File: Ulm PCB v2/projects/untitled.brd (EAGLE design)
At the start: 56.6 x 49.2 mm, 26 parts, among them U1 FT232RLSSOP, U2 MCP73831, U3 SPX3819-3.3, U4 RFM69HCW, X2 USB-SMD-NS

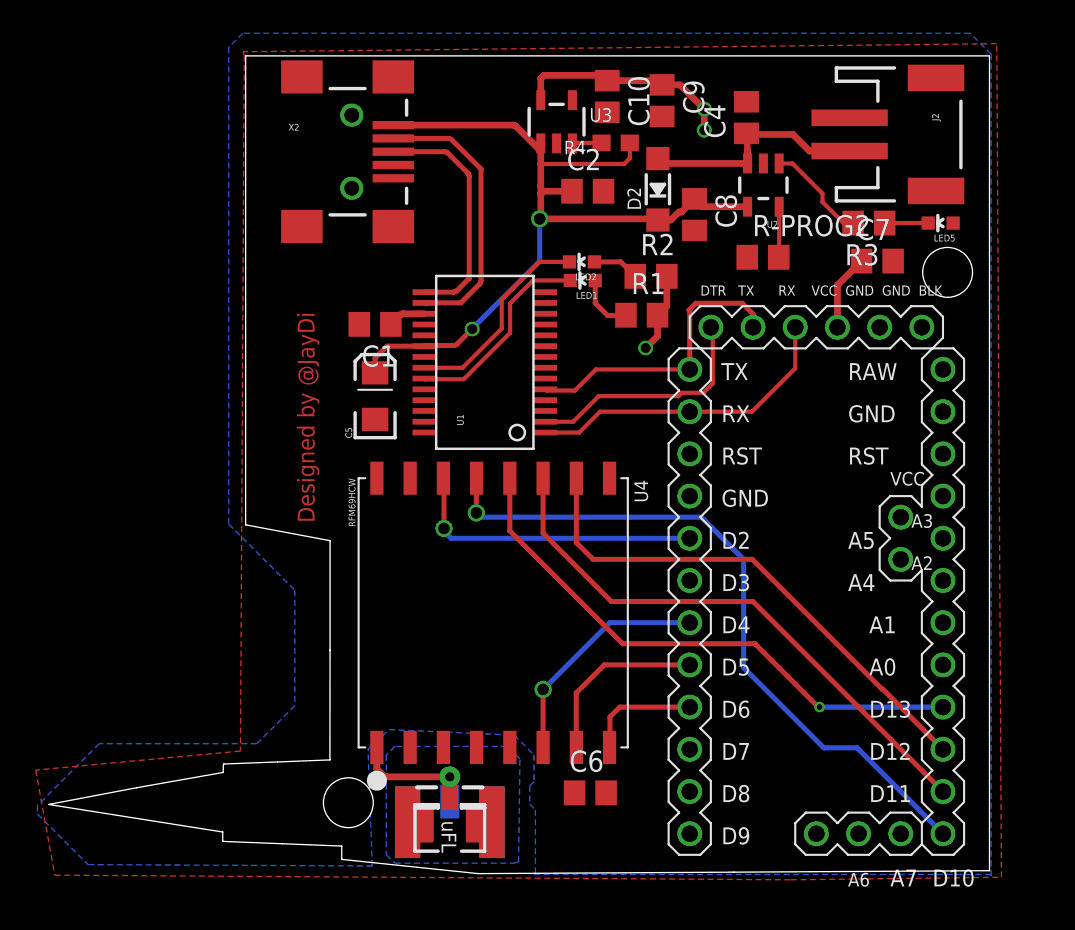
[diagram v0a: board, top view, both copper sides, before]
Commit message: corrected DRC-Errors. ToDo: Right USB Slot, Diode vs. Jumper
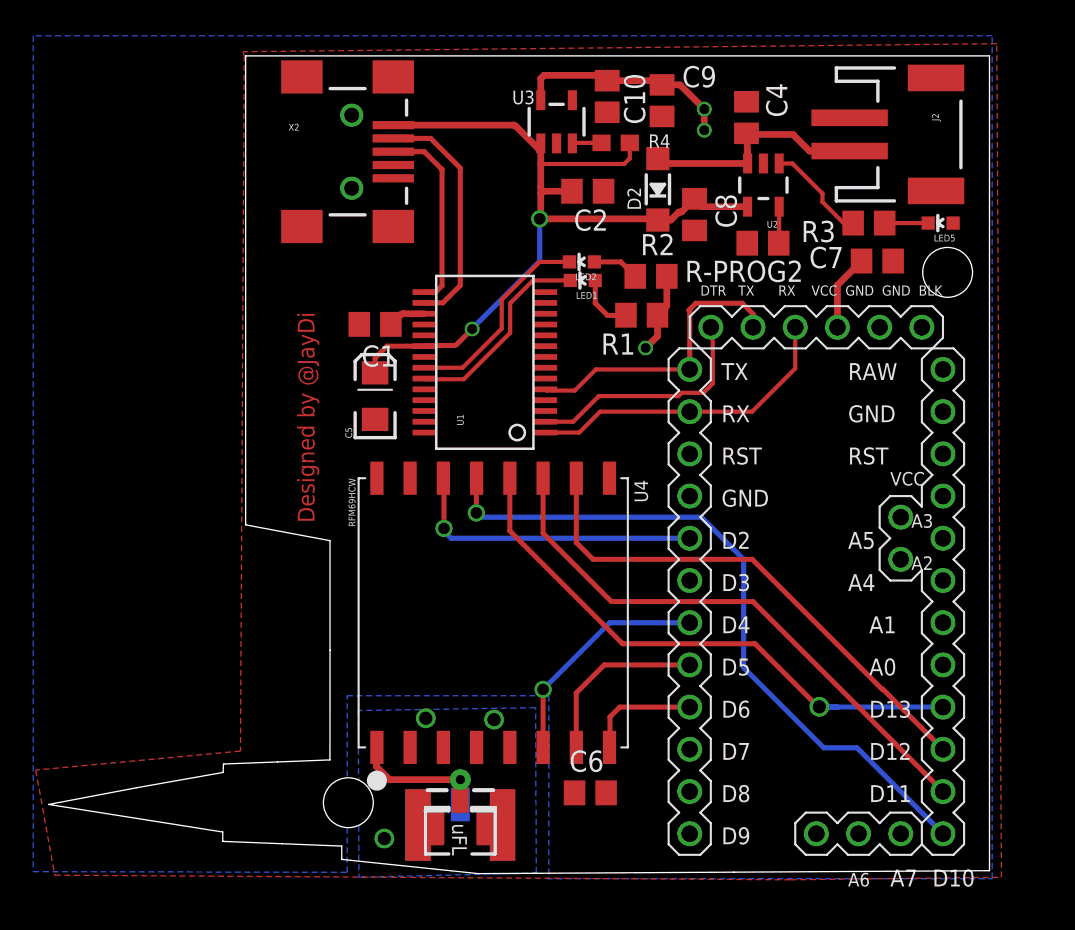
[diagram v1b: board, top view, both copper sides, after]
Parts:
- moved R-PROG2 0.85 mm to (43.9, 39.2)
- moved J$2 0.66 mm to (25.7, 1.81)
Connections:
- removed net N$4: J$2.ANT1, J$2.ANT2, J$2.ANT3
- new net ANT: J$2.ANT1, J$2.ANT2, J$2.ANT3, U4.1P
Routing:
- net ANT: track 0.00 -> 9.27 mm
- net N$4: track 8.95 -> 0.00 mm
- net USB_D+: track 14.4 -> 11.7 mm
- net USB_D-: track 16.8 -> 14.5 mm
- net SCL: track 33.6 -> 34.8 mm
- net LOL: track 3.04 -> 2.20 mm
- net GND: vias 0 -> 3

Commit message: Final Final
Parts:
- added D3: MBR120, microbuilder:SOD-123
- moved C2 4.78 mm to (28.8, 41.1), turned to 270 degrees
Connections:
- removed net 5V: C2.1, C5.A, C8.1, D2.C, R4.1, U1.20, U2.4, U3.1, X2.VBUS
- new net V5: C8.1, D2.C, D3.C, R4.1, U2.4, U3.1
- new net VBUS: C2.1, C5.A, D3.A, U1.20, X2.VBUS
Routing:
- net 5V: track 51.7 -> 0.00 mm, vias 2 -> 0
- net VBUS: track 0.00 -> 27.8 mm, vias 0 -> 2
- net V5: track 0.00 -> 26.5 mm
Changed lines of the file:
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@@
 <elements>
 <element name="C1" library="rcl" library_urn="urn:adsk.eagle:library:334" package="C0805" value="0.1uF" x="20.574" y="34.29" rot="R180"/>
-<element name="C2" library="rcl" library_urn="urn:adsk.eagle:library:334" package="C0805" value="0.1uF" x="33.3733875" y="42.30069375" smashed="yes">
-<attribute name="NAME" x="32.526803125" y="39.9293" size="1.27" layer="25"/>
-<attribute name="VALUE" x="32.1033875" y="39.76069375" size="1.27" layer="27"/>
+<element name="C2" library="rcl" library_urn="urn:adsk.eagle:library:334" package="C0805" value="0.1uF" x="28.75131875" y="41.063496875" smashed="yes" rot="R270">
+<attribute name="NAME" x="26.379925" y="41.91008125" size="1.27" layer="25" rot="R270"/>
+<attribute name="VALUE" x="26.21131875" y="42.333496875" size="1.27" layer="27" rot="R270"/>
 </element>
 <element name="C5" library="SparkFun" package="EIA3216" value="10uF" x="20.574" y="29.972" rot="R90"/>
@@
 <element name="J$2" library="_c2h" package="SMA_UFL_PAD_TINY" value="ANTENNATINY" x="25.704928125" y="1.811834375" rot="R270"/>
 <element name="U4" library="microbuilder" package="RFMHCW_SMT" value="RFM69HCW" x="27.683234375" y="16.9316375" rot="R270"/>
+<element name="D3" library="microbuilder" package="SOD-123" value="MBR120" x="25.997865625" y="47.422815625" rot="R180"/>
 </elements>
 <signals>
@@
 <contactref element="U1" pad="4"/>
 </signal>
-<signal name="5V">
-<contactref element="U1" pad="20"/>
-<contactref element="C5" pad="A"/>
-<contactref element="C2" pad="1"/>
-<contactref element="X2" pad="VBUS"/>
-<contactref element="C8" pad="1"/>
-<contactref element="U3" pad="1"/>
-<contactref element="D2" pad="C"/>
-<contactref element="R4" pad="1"/>
-<contactref element="U2" pad="4"/>
-<wire x1="30.513953125" y1="45.213946875" x2="30.546" y2="45.1819" width="0.4064" layer="1"/>
-<wire x1="30.546" y1="44.716071875" x2="30.546" y2="45.1819" width="0.4064" layer="1"/>
-<wire x1="30.546" y1="44.716071875" x2="30.546" y2="43.942" width="0.4064" layer="1"/>
-<wire x1="30.546" y1="43.942" x2="30.546" y2="42.606" width="0.4064" layer="1"/>
-<wire x1="35.902" y1="45.212" x2="35.902" y2="44.284" width="0.254" layer="1"/>
-<wire x1="35.902" y1="44.284" x2="35.56" y2="43.942" width="0.254" layer="1"/>
-<wire x1="35.56" y1="43.942" x2="30.546" y2="43.942" width="0.254" layer="1"/>
-<wire x1="20.574" y1="31.372" x2="20.657" y2="31.455" width="0.254" layer="1"/>
-<wire x1="30.48" y1="42.54" x2="30.546" y2="42.606" width="0.3048" layer="1"/>
-<via x="30.48" y="40.64" extent="1-16" drill="0.7"/>
-<wire x1="39.798" y1="41.835359375" x2="39.798" y2="41.844" width="0.4064" layer="1"/>
-<wire x1="42.992" y1="41.3719" x2="40.261459375" y2="41.3719" width="0.4064" layer="1"/>
-<wire x1="40.261459375" y1="41.3719" x2="39.798" y2="41.835359375" width="0.4064" layer="1"/>
-<wire x1="38.85861875" y1="41.0512" x2="39.013840625" y2="41.0512" width="0.4064" layer="1"/>
-<wire x1="39.013840625" y1="41.0512" x2="39.798" y2="41.835359375" width="0.4064" layer="1"/>
-<wire x1="37.592" y1="40.568" x2="38.37541875" y2="40.568" width="0.4064" layer="1"/>
-<wire x1="38.37541875" y1="40.568" x2="38.85861875" y2="41.0512" width="0.4064" layer="1"/>
-<wire x1="30.546" y1="42.16411875" x2="30.546" y2="42.606" width="0.4064" layer="1"/>
-<wire x1="30.546" y1="42.16411875" x2="30.546" y2="40.706" width="0.4064" layer="1"/>
-<wire x1="30.48" y1="40.64" x2="37.52" y2="40.64" width="0.4064" layer="1"/>
-<wire x1="37.52" y1="40.64" x2="37.592" y2="40.568" width="0.4064" layer="1"/>
-<via x="26.416" y="34.0106" extent="1-16" drill="0.6"/>
-<wire x1="30.48" y1="38.1" x2="30.48" y2="40.64" width="0.3048" layer="16"/>
-<wire x1="30.546" y1="40.706" x2="30.48" y2="40.64" width="0.4064" layer="1"/>
-<wire x1="32.4233875" y1="42.30069375" x2="30.682575" y2="42.30069375" width="0.4064" layer="1"/>
-<wire x1="30.682575" y1="42.30069375" x2="30.546" y2="42.16411875" width="0.4064" layer="1"/>
-<wire x1="21.295" y1="32.979" x2="20.574" y2="32.258" width="0.3048" layer="1"/>
-<wire x1="20.574" y1="32.258" x2="20.574" y2="31.372" width="0.3048" layer="1"/>
-<wire x1="23.522" y1="32.979" x2="23.563" y2="33.02" width="0.3048" layer="1"/>
-<wire x1="23.522" y1="32.979" x2="21.295" y2="32.979" width="0.3048" layer="1"/>
-<wire x1="25.320190625" y1="33.02" x2="25.49979375" y2="33.09439375" width="0.3048" layer="1" curve="44.999502"/>
-<wire x1="25.49979375" y1="33.09439375" x2="26.416" y2="34.0106" width="0.3048" layer="1"/>
-<wire x1="23.563" y1="33.02" x2="25.320190625" y2="33.02" width="0.3048" layer="1"/>
-<wire x1="26.416" y1="34.0106" x2="26.433959375" y2="34.053959375" width="0.3048" layer="16" curve="-44.997935"/>
-<wire x1="26.433959375" y1="34.053959375" x2="30.48" y2="38.1" width="0.3048" layer="16"/>
-<wire x1="21.669625" y1="46.280746875" x2="28.876115625" y2="46.280746875" width="0.4064" layer="1"/>
-<wire x1="28.876115625" y1="46.280746875" x2="29.05571875" y2="46.206353125" width="0.4064" layer="1" curve="-44.999502"/>
-<wire x1="29.05571875" y1="46.206353125" x2="30.546" y2="44.716071875" width="0.4064" layer="1"/>
-</signal>
 <signal name="SCL">
 <contactref element="U$1" pad="D13"/>
@@
 <wire x1="20.662796875" y1="8.8112" x2="20.683234375" y2="8.8316375" width="0.4064" layer="1"/>
 </signal>
+<signal name="VBUS">
+<contactref element="U1" pad="20"/>
+<contactref element="C5" pad="A"/>
+<contactref element="C2" pad="1"/>
+<contactref element="X2" pad="VBUS"/>
+<wire x1="20.574" y1="31.372" x2="20.657" y2="31.455" width="0.254" layer="1"/>
+<wire x1="21.295" y1="32.979" x2="20.574" y2="32.258" width="0.3048" layer="1"/>
+<wire x1="20.574" y1="32.258" x2="20.574" y2="31.372" width="0.3048" layer="1"/>
+<wire x1="23.522" y1="32.979" x2="21.295" y2="32.979" width="0.3048" layer="1"/>
+<contactref element="D3" pad="A"/>
+<wire x1="22.81169375" y1="47.422815625" x2="24.147865625" y2="47.422815625" width="0.4064" layer="1"/>
+<wire x1="21.669625" y1="46.280746875" x2="22.81169375" y2="47.422815625" width="0.4064" layer="1"/>
+<wire x1="24.147865625" y1="47.422815625" x2="24.147865625" y2="46.393571875" width="0.4064" layer="1"/>
+<wire x1="27.056409375" y1="43.485028125" x2="27.01406875" y2="43.485028125" width="0.4064" layer="1"/>
+<wire x1="26.971728125" y1="43.4426875" x2="27.01406875" y2="43.485028125" width="0.4064" layer="1"/>
+<via x="26.971728125" y="43.4426875" extent="1-16" drill="0.6"/>
+<wire x1="24.147865625" y1="46.393571875" x2="27.056409375" y2="43.485028125" width="0.4064" layer="1"/>
+<wire x1="26.971728125" y1="43.4426875" x2="26.971728125" y2="34.720278125" width="0.4064" layer="16"/>
+<wire x1="26.971728125" y1="34.720278125" x2="25.2357125" y2="32.9842625" width="0.4064" layer="16"/>
+<wire x1="25.2357125" y1="32.9842625" x2="25.278053125" y2="32.9842625" width="0.4064" layer="16"/>
+<via x="25.278053125" y="32.9842625" extent="1-16" drill="0.6"/>
+<wire x1="25.278053125" y1="32.9842625" x2="23.5272625" y2="32.9842625" width="0.3048" layer="1"/>
+<wire x1="23.5272625" y1="32.9842625" x2="23.522" y2="32.979" width="0.3048" layer="1"/>
+<wire x1="28.75131875" y1="42.013496875" x2="28.40091875" y2="42.013496875" width="0.3048" layer="1"/>
+<wire x1="28.40091875" y1="42.013496875" x2="26.971728125" y2="43.4426875" width="0.3048" layer="1"/>
+</signal>
+<signal name="V5">
+<contactref element="U2" pad="4"/>
+<contactref element="C8" pad="1"/>
+<contactref element="U3" pad="1"/>
+<contactref element="D2" pad="C"/>
+<contactref element="R4" pad="1"/>
+<wire x1="30.513953125" y1="45.213946875" x2="30.546" y2="45.1819" width="0.4064" layer="1"/>
+<wire x1="30.546" y1="44.716071875" x2="30.546" y2="45.1819" width="0.4064" layer="1"/>
+<wire x1="30.546" y1="43.942" x2="30.546" y2="44.716071875" width="0.4064" layer="1"/>
+<wire x1="35.902" y1="45.212" x2="35.902" y2="44.284" width="0.254" layer="1"/>
+<wire x1="35.902" y1="44.284" x2="35.56" y2="43.942" width="0.254" layer="1"/>
+<wire x1="35.56" y1="43.942" x2="30.546" y2="43.942" width="0.254" layer="1"/>
+<wire x1="39.798" y1="41.835359375" x2="39.798" y2="41.844" width="0.4064" layer="1"/>
+<wire x1="39.97646875" y1="41.656890625" x2="40.261459375" y2="41.3719" width="0.4064" layer="1"/>
+<wire x1="39.97646875" y1="41.656890625" x2="39.798" y2="41.835359375" width="0.4064" layer="1"/>
+<wire x1="38.85861875" y1="41.0512" x2="39.013840625" y2="41.0512" width="0.4064" layer="1"/>
+<wire x1="39.013840625" y1="41.0512" x2="39.798" y2="41.835359375" width="0.4064" layer="1"/>
+<wire x1="38.37541875" y1="40.568" x2="37.592" y2="40.568" width="0.4064" layer="1"/>
+<wire x1="38.37541875" y1="40.568" x2="38.85861875" y2="41.0512" width="0.4064" layer="1"/>
+<wire x1="30.546" y1="44.716071875" x2="29.05571875" y2="46.206353125" width="0.4064" layer="1"/>
+<contactref element="D3" pad="C"/>
+<wire x1="29.05571875" y1="46.206353125" x2="29.05571875" y2="46.2149625" width="0.4064" layer="1"/>
+<wire x1="29.05571875" y1="46.2149625" x2="27.847865625" y2="47.422815625" width="0.4064" layer="1"/>
+<wire x1="37.592" y1="40.568" x2="33.92" y2="40.568" width="0.4064" layer="1"/>
+<wire x1="33.92" y1="40.568" x2="30.546" y2="43.942" width="0.4064" layer="1"/>
+<wire x1="42.992" y1="41.3719" x2="40.261459375" y2="41.3719" width="0.4064" layer="1"/>
+<wire x1="40.261459375" y1="41.3719" x2="39.97646875" y2="41.656890625" width="0.4064" layer="1"/>
+</signal>
 </signals>
